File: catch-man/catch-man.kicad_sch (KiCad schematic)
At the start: 23 parts, among them Q1 2N3904, SW1 SW_Push_45deg, SW2 SW_SPDT, U1 STC8G1K08A-36I-DFN8

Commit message: catch-man: v1
Finished layout, centered parts
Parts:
- added C1: 0.1u, Capacitor_THT:C_Disc_D3.0mm_W1.6mm_P2.50mm, symbol Device:C
- LS1: value Speaker -> 9024 Passive Buzzer; footprint Buzzer_Beeper:Buzzer_12x9.5RM7.6 -> Buzzer_Beeper:MagneticBuzzer_PUI_AT-0927-TT-6-R
- Q1: value 2N3904 -> 2N2222; footprint Package_TO_SOT_THT:TO-92_Inline -> Package_TO_SOT_THT:TO-18-3; symbol Transistor_BJT:2N3904 -> Transistor_BJT:PN2222A
- SW2: value SW_SPDT -> POWER
- U1: value STC8G1K08A-36I-DFN8 -> STC8G1K08A-36I-DIP8
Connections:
- net GND: now also C1.2
- net VCC: now reaches LS1.1, SW2.1 (A), U1.2 (VCC)
- net VCC: now also C1.1
- no-connect marks 0 -> 2

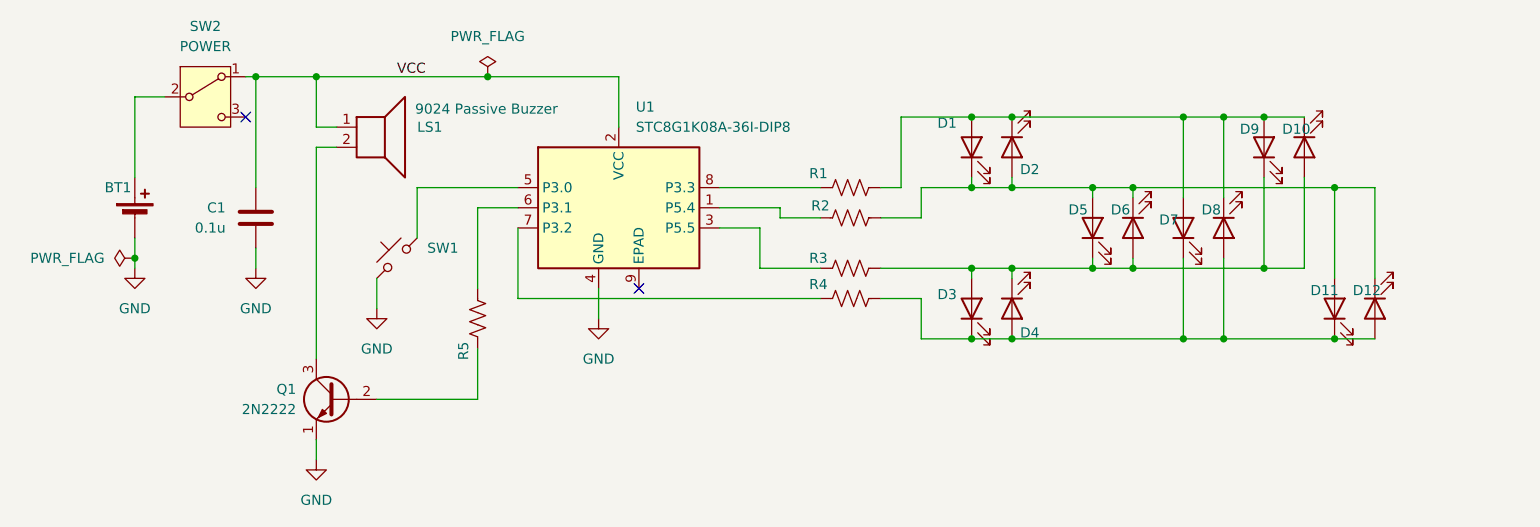
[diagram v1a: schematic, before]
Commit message: catch-man v1: done, ordered
Add 2nd footprint for speaker - not sure which one will work
best

Add README.md
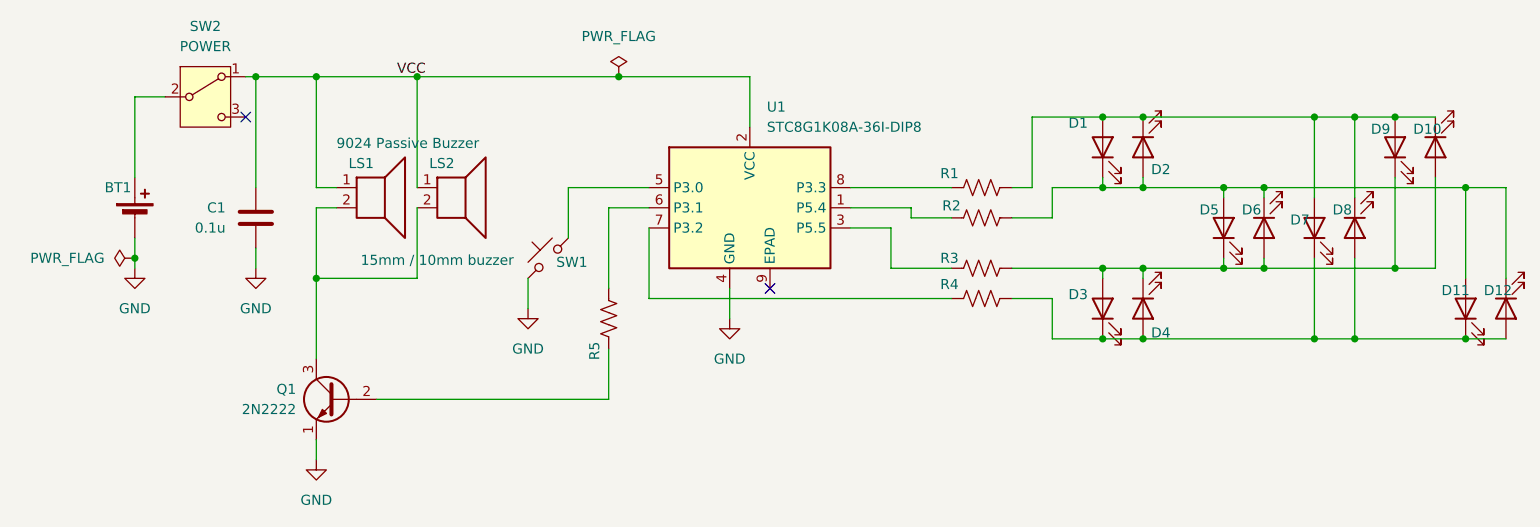
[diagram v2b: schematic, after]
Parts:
- added LS2: 15mm / 10mm buzzer, Buzzer_Beeper:Buzzer_D14mm_H7mm_P10mm, symbol Device:Speaker
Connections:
- net VCC: now also LS2.1
- net at LS1.2, Q1.3 (C): now also LS2.2
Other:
- moved on the sheet: D1, D10, D11, D12, D2, D3, D4, D5, D6, D7, D8, D9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

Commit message: catch-man: start on board redesign
To keep things simple, don't change connection pinout, duplicate
manual changes on existing protype

The "catch-man" caption is not big enough yet, we'll want to move it
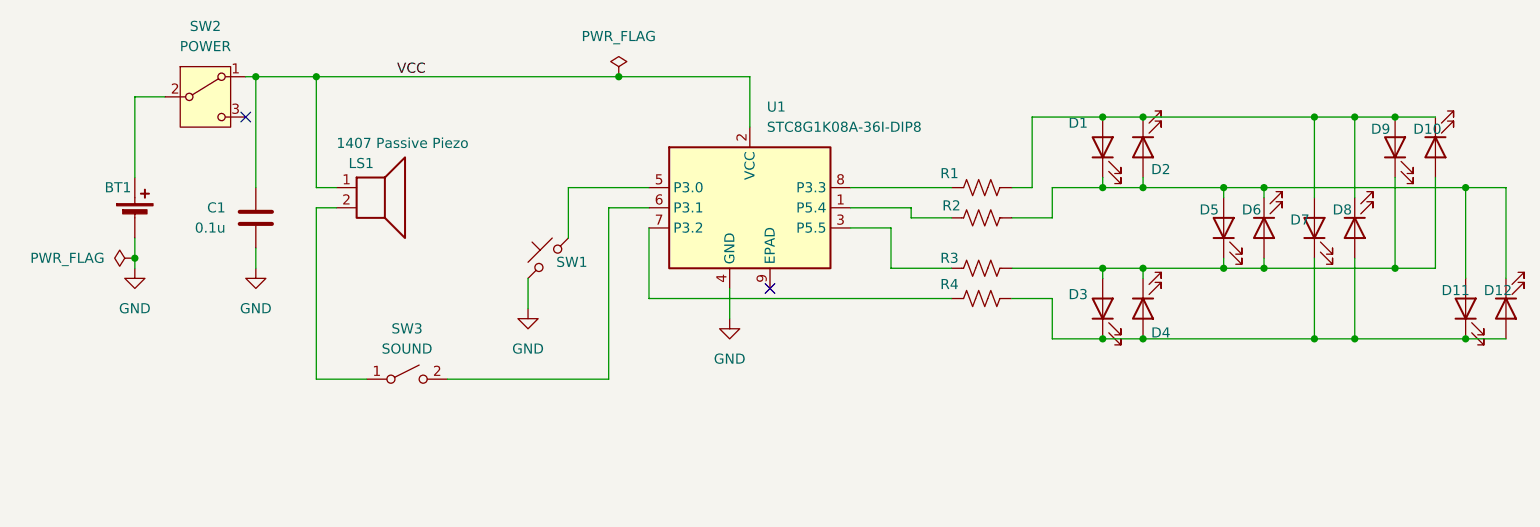
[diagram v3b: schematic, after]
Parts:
- removed LS2: 15mm / 10mm buzzer, Buzzer_Beeper:Buzzer_D14mm_H7mm_P10mm, symbol Device:Speaker
- removed Q1: 2N2222, Package_TO_SOT_THT:TO-18-3, symbol Transistor_BJT:PN2222A
- removed R5: 120, Resistor_THT:R_Axial_DIN0204_L3.6mm_D1.6mm_P7.62mm_Horizontal, symbol Device:R_US
- added SW3: SOUND, Button_Switch_THT:SW_DIP_SPSTx01_Slide_9.78x4.72mm_W7.62mm_P2.54mm, symbol Switch:SW_SPST
- LS1: value 9024 Passive Buzzer -> 1407 Passive Piezo; footprint Buzzer_Beeper:MagneticBuzzer_PUI_AT-0927-TT-6-R -> Buzzer_Beeper:Buzzer_15x7.5RM7.6
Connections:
- net at U1.6 (P3.1): now also SW3.2 (B)
- net at LS1.2: now also SW3.1 (A)
